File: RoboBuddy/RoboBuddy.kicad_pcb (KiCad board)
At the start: 2 copper layers, 32 x 21 mm, 33 parts, among them J1 USB_B_Micro, J3 Micro_SD_Card, U1 RP2040, U2 NCP1117-3.3_SOT223, U3 W25Q128JVS, U4 LSM6DS3, Y1 ABM8-272-T3

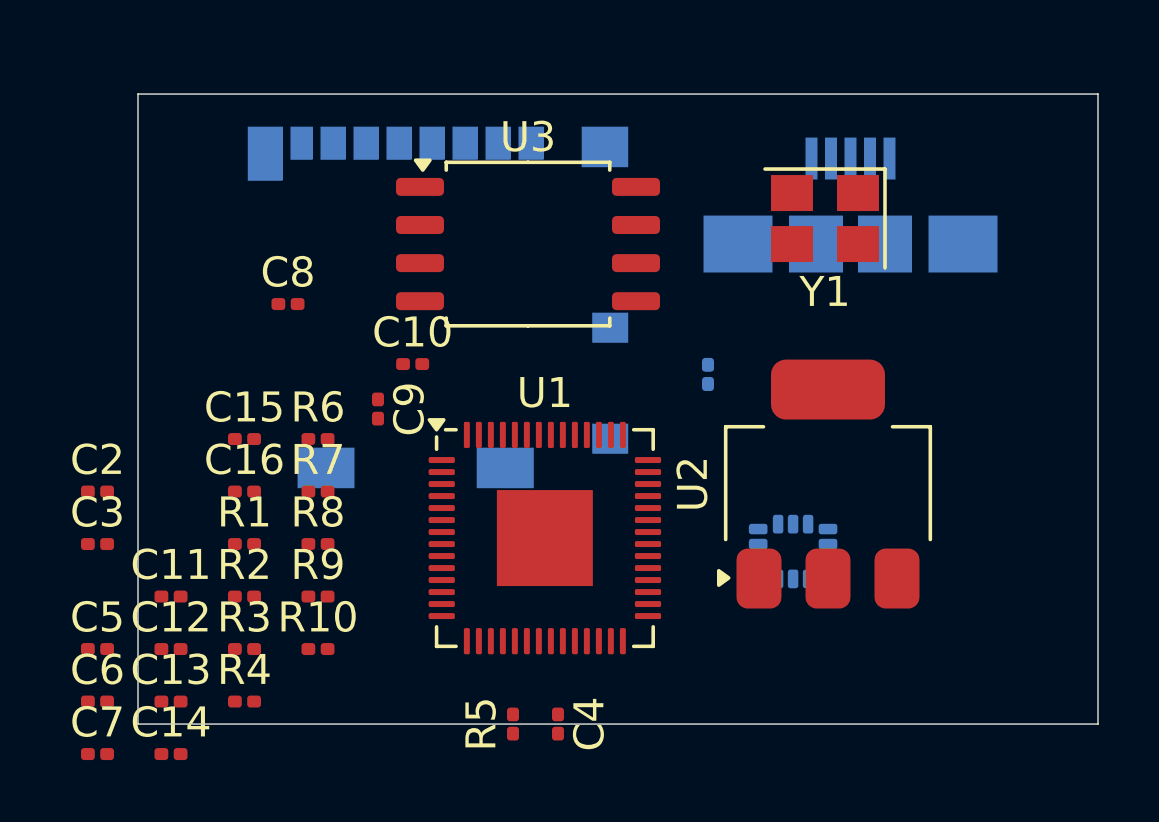
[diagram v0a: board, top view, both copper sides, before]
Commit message: Add files via upload
Finished the connecting everything on the pcb schematic. I will now get rid of some of the overlapping silkscreen (mainly getting rid of the capacitors and resistors tags)
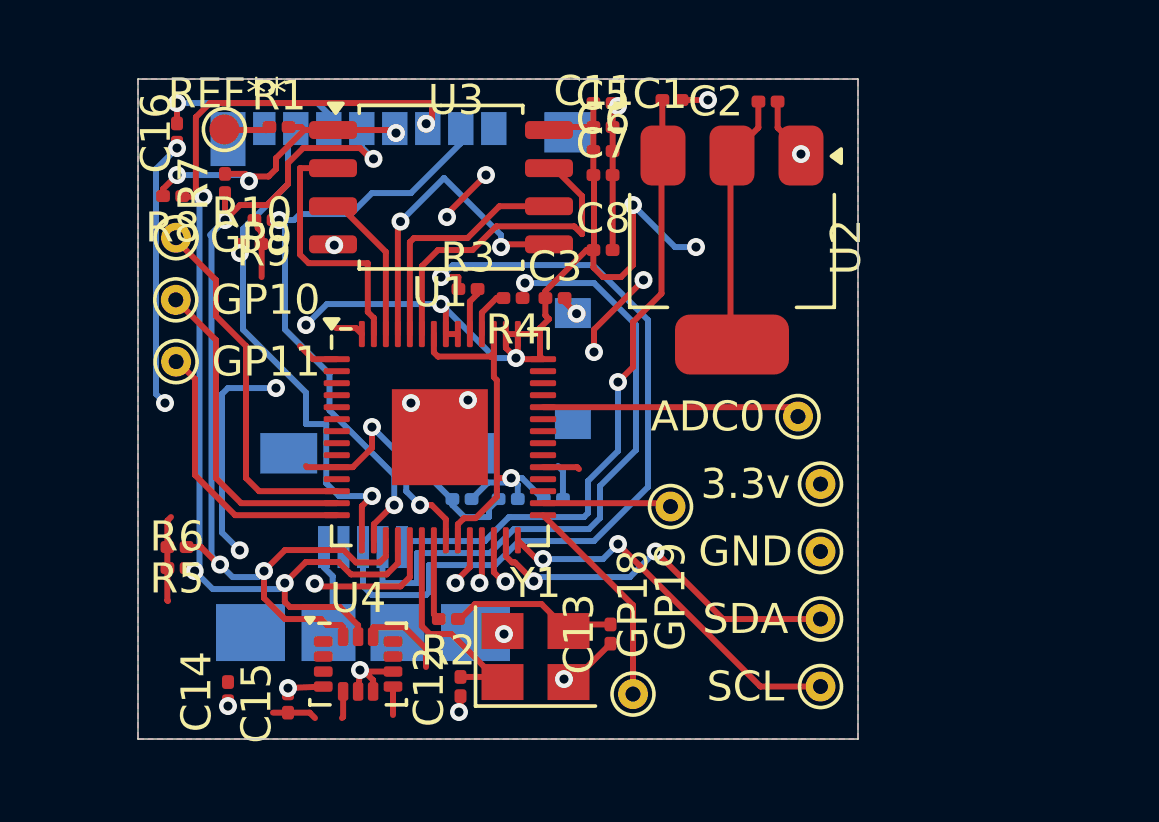
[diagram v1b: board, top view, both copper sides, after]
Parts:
- added 3.3v: TestPoint_THTPad_D1.0mm_Drill0.5mm, TestPoint:TestPoint_THTPad_D1.0mm_Drill0.5mm, F.Cu at (158.8, 91.0)
- added ADC0: TestPoint_THTPad_D1.0mm_Drill0.5mm, TestPoint:TestPoint_THTPad_D1.0mm_Drill0.5mm, F.Cu at (158.0, 88.8)
- added GND: TestPoint_THTPad_D1.0mm_Drill0.5mm, TestPoint:TestPoint_THTPad_D1.0mm_Drill0.5mm, F.Cu at (158.8, 93.2)
- added GP10: TestPoint_THTPad_D1.0mm_Drill0.5mm, TestPoint:TestPoint_THTPad_D1.0mm_Drill0.5mm, F.Cu at (137.3, 84.9)
- added GP11: TestPoint_THTPad_D1.0mm_Drill0.5mm, TestPoint:TestPoint_THTPad_D1.0mm_Drill0.5mm, F.Cu at (137.3, 86.9)
- added GP18: TestPoint_THTPad_D1.0mm_Drill0.5mm, TestPoint:TestPoint_THTPad_D1.0mm_Drill0.5mm, F.Cu at (152.5, 98.0)
- added GP19: TestPoint_THTPad_D1.0mm_Drill0.5mm, TestPoint:TestPoint_THTPad_D1.0mm_Drill0.5mm, F.Cu at (153.8, 91.8)
- added GP9: TestPoint_THTPad_D1.0mm_Drill0.5mm, TestPoint:TestPoint_THTPad_D1.0mm_Drill0.5mm, F.Cu at (137.3, 82.8)
- added REF**: TestPoint_Pad_D1.0mm, TestPoint:TestPoint_Pad_D1.0mm, F.Cu at (138.9, 79.2)
- added SCL: TestPoint_THTPad_D1.0mm_Drill0.5mm, TestPoint:TestPoint_THTPad_D1.0mm_Drill0.5mm, F.Cu at (158.8, 97.8)
- added SDA: TestPoint_THTPad_D1.0mm_Drill0.5mm, TestPoint:TestPoint_THTPad_D1.0mm_Drill0.5mm, F.Cu at (158.8, 95.5)
- C1, U4: moved to F.Cu
- C10, C4, C9: moved to B.Cu
- moved C2 25.9 mm to (157.0, 78.2)
- moved C7 25.6 mm to (151.5, 80.7)
- moved C6 24.9 mm to (151.5, 79.9)
- moved C5 24.2 mm to (151.5, 79.1)
- moved C11 21.9 mm to (151.5, 78.3)
- moved J1 20.8 mm to (143.5, 94.7)
- moved Y1 17.5 mm to (149.2, 96.8), turned to 0 degrees
- moved C3 17.3 mm to (149.9, 84.8)
- moved R4 16.2 mm to (148.5, 84.8), turned to 180 degrees
- moved U4 15.0 mm to (143.3, 97.0), turned to 0 degrees
- moved C13 14.8 mm to (151.8, 96.0), turned to 90 degrees
- moved R3 14.1 mm to (147.0, 84.5)
- moved R1 13.9 mm to (140.7, 79.1)
- moved R10 13.7 mm to (139.8, 83.0)
- moved R9 12.7 mm to (140.2, 82.2), turned to 180 degrees
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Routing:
- net +3.3V: track 0.00 -> 80.9 mm, vias 0 -> 12
- net GND: track 0.00 -> 39.6 mm, vias 0 -> 19
- net /SCL_GRYO/MOSI_SD: track 0.00 -> 37.6 mm, vias 0 -> 4
- net /SDA_GYRO/SCK_SD: track 0.00 -> 33.6 mm, vias 0 -> 4
- net /USB_D+: track 0.00 -> 27.5 mm, vias 0 -> 1
- net /USB_D-: track 0.00 -> 22.0 mm, vias 0 -> 1
- net VBUS: track 0.00 -> 21.4 mm, vias 0 -> 1
- net /CS_SD: track 0.00 -> 20.4 mm, vias 0 -> 2
- net /MISO_SD: track 0.00 -> 17.8 mm, vias 0 -> 2
- net +1V1: track 0.00 -> 15.3 mm, vias 0 -> 1
- net /SDA_OLED: track 0.00 -> 12.7 mm, vias 0 -> 2
- net /SCL_OLED: track 0.00 -> 12.5 mm, vias 0 -> 2
- net /GPIO_9: track 0.00 -> 12.2 mm
- net /QSPI_SD3: track 0.00 -> 11.0 mm
- net /GPIO_10: track 0.00 -> 11.0 mm
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- added copper zone on F.Cu, net +3.3V
- added copper zone on B.Cu, net GND
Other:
- board size 32 x 21 mm -> 24 x 22 mm
